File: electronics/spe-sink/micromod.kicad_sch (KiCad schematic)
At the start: 5 parts, among them IC1 AT24C02C-SSHM, X2 MICROMOD_FUNCTION_BOARD_EDGE

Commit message: PD function board schematic progress
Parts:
- C20: footprint CAPC1608* -> Applidyne_Capacitor:CAPC1608X90N
- X2: footprint (none) -> Applidyne_Connector:M.2-MICROMOD-FN-CARD-EDGE
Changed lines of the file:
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@@
       (effects (font (size 1.524 1.524) bold))
     )
-    (property "Footprint" "" (at 156.21 157.48 0)
+    (property "Footprint" "Applidyne_Connector:M.2-MICROMOD-FN-CARD-EDGE" (at 156.21 157.48 0)
       (effects (font (size 0.9906 0.9906)) (justify left bottom) hide)
     )
@@
       (effects (font (size 0.889 0.889)) (justify left))
     )
-    (property "Footprint" "CAPC1608*" (at 61.849 67.31 90)
+    (property "Footprint" "Applidyne_Capacitor:CAPC1608X90N" (at 61.849 67.31 90)
       (effects (font (size 0.508 0.508)) hide)
     )

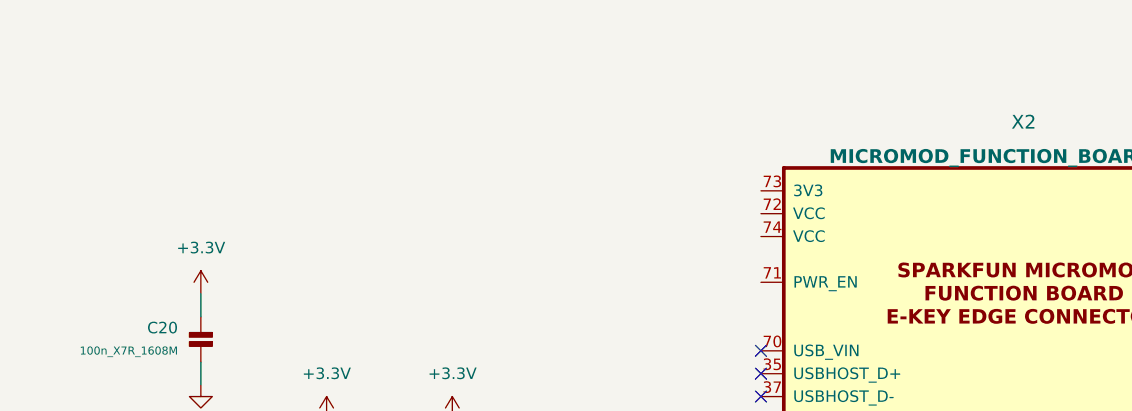
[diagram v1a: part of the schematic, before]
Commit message: PD function board bulk regulator, cleanup, part placement
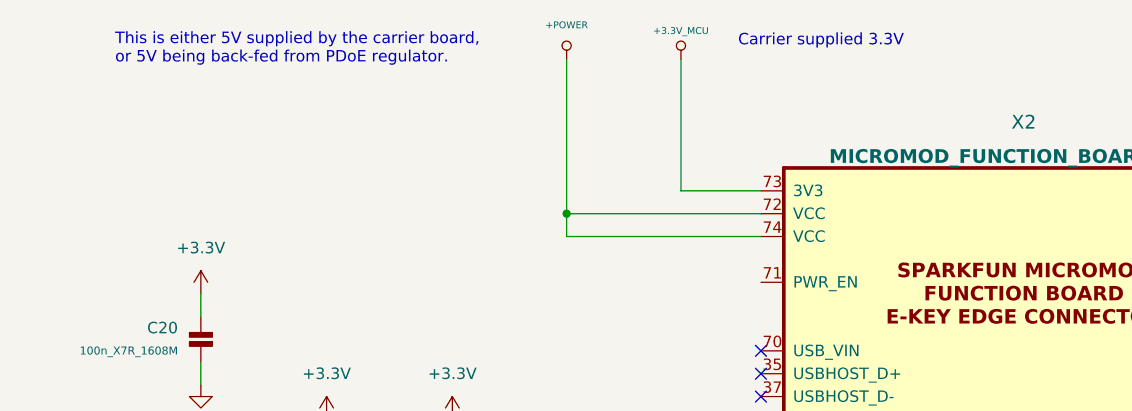
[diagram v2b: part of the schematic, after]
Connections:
- net +POWER: now reaches X2.72 (VCC)
- net +POWER: now also X2.74 (VCC)
- net +3.3V_MCU: now reaches X2.73 (3V3)
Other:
- note added: "Carrier supplied 3.3V"
- note added: "This is either 5V supplied by the carrier board, or 5V being back-fed from PDoE regulator."
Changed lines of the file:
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@@
   (junction (at 123.19 121.92) (diameter 0) (color 0 0 0 0)
+  )
+  (junction (at 105.41 53.34) (diameter 0) (color 0 0 0 0)
   )
   (junction (at 92.71 97.79) (diameter 0) (color 0 0 0 0)
@@
     (stroke (width 0) (type default))
   )
+  (wire (pts (xy 105.41 53.34) (xy 127 53.34))
+    (stroke (width 0) (type default))
+  )
   (wire (pts (xy 185.42 116.84) (xy 215.9 116.84))
     (stroke (width 0) (type default))
@@
     (stroke (width 0) (type default))
   )
+  (wire (pts (xy 127 50.8) (xy 118.11 50.8))
+    (stroke (width 0) (type default))
+  )
   (wire (pts (xy 123.19 129.54) (xy 127 129.54))
     (stroke (width 0) (type default))
@@
     (stroke (width 0) (type default))
   )
+  (wire (pts (xy 118.11 36.195) (xy 118.11 50.8))
+    (stroke (width 0) (type default))
+  )
   (bus (pts (xy 207.01 68.58) (xy 220.98 68.58))
     (stroke (width 0) (type default))
@@
     (stroke (width 0) (type default))
   )
+  (wire (pts (xy 105.41 55.88) (xy 105.41 53.34))
+    (stroke (width 0) (type default))
+  )
+  (wire (pts (xy 105.41 53.34) (xy 105.41 36.195))
+    (stroke (width 0) (type default))
+  )
+  (wire (pts (xy 127 55.88) (xy 105.41 55.88))
+    (stroke (width 0) (type default))
+  )
   (wire (pts (xy 92.71 106.68) (xy 92.71 107.95))
     (stroke (width 0) (type default))
@@
   (bus (pts (xy 207.01 55.88) (xy 207.01 53.34))
     (stroke (width 0) (type default))
+  )
+  (text "Carrier supplied 3.3V" (at 124.46 34.925 0)
+    (effects (font (size 1.27 1.27)) (justify left bottom))
+  )
+  (text "This is either 5V supplied by the carrier board,\nor 5V being back-fed from PDoE regulator."
+    (at 55.245 36.83 0)
+    (effects (font (size 1.27 1.27)) (justify left bottom))
   )
   (text "Write protected when high" (at 119.38 100.33 0)
@@
     )
   )
+  (symbol (lib_id "appli_power:+POWER") (at 105.41 36.195 0) (unit 1)
+    (in_bom yes) (on_board yes) (dnp no) (fields_autoplaced)
+    (property "Reference" "#PWR054" (at 105.41 37.465 0)
+      (effects (font (size 0.508 0.508)) hide)
+    )
+    (property "Value" "+POWER" (at 105.41 32.385 0)
+      (effects (font (size 0.762 0.762)))
+    )
+    (property "Footprint" "" (at 105.41 36.195 0)
+      (effects (font (size 1.524 1.524)))
+    )
+    (property "Datasheet" "" (at 105.41 36.195 0)
+      (effects (font (size 1.524 1.524)))
+    )
+    (pin "1")
+    (instances
+      (project "spe-sink"
+        (path "/f0a501c7-1ad1-4c59-9255-3d6aa4545d8b/d2c298ab-d4a2-4c33-86fb-9b17f2cedd7c"
+          (reference "#PWR054") (unit 1)
+        )
+        (path "/f0a501c7-1ad1-4c59-9255-3d6aa4545d8b/4db035f6-4a09-4a2b-8e2e-a64ccd99d7de"
+          (reference "#PWR024") (unit 1)
+        )
+      )
+    )
+  )
   (symbol (lib_id "appli_power:+3.3V") (at 78.74 76.2 0) (mirror y) (unit 1)
     (in_bom yes) (on_board yes) (dnp no) (fields_autoplaced)
@@
         )
       )
+    )
+  )
+  (symbol (lib_id "appli_power:+3.3V_MCU") (at 118.11 36.195 0) (unit 1)
+    (in_bom yes) (on_board yes) (dnp no) (fields_autoplaced)
+    (property "Reference" "#PWR055" (at 118.11 37.211 0)
+      (effects (font (size 0.762 0.762)) hide)
+    )
+    (property "Value" "+3.3V_MCU" (at 118.11 33.02 0)
+      (effects (font (size 0.762 0.762)))
+    )
+    (property "Footprint" "" (at 118.11 36.195 0)
+      (effects (font (size 1.524 1.524)))
+    )
+    (property "Datasheet" "" (at 118.11 36.195 0)
+      (effects (font (size 1.524 1.524)))
+    )
+    (pin "1")
+    (instances
+      (project "spe-sink"
+        (path "/f0a501c7-1ad1-4c59-9255-3d6aa4545d8b/4db035f6-4a09-4a2b-8e2e-a64ccd99d7de"
+          (reference "#PWR055") (unit 1)
+        )
+      )

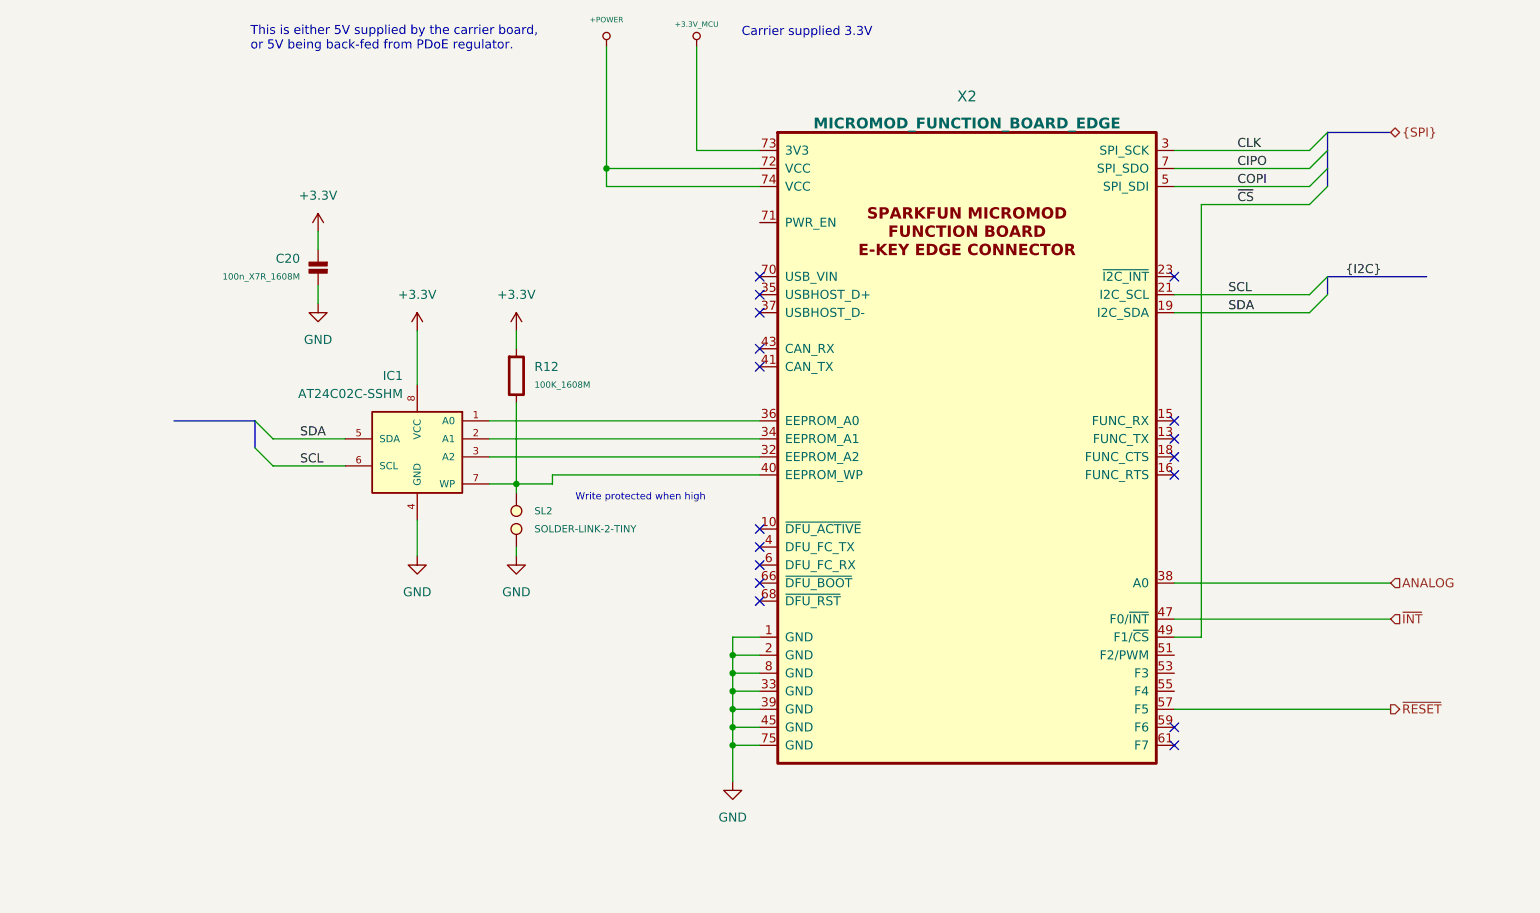
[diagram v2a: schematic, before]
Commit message: PD sink board routing, minor sch changes, etc
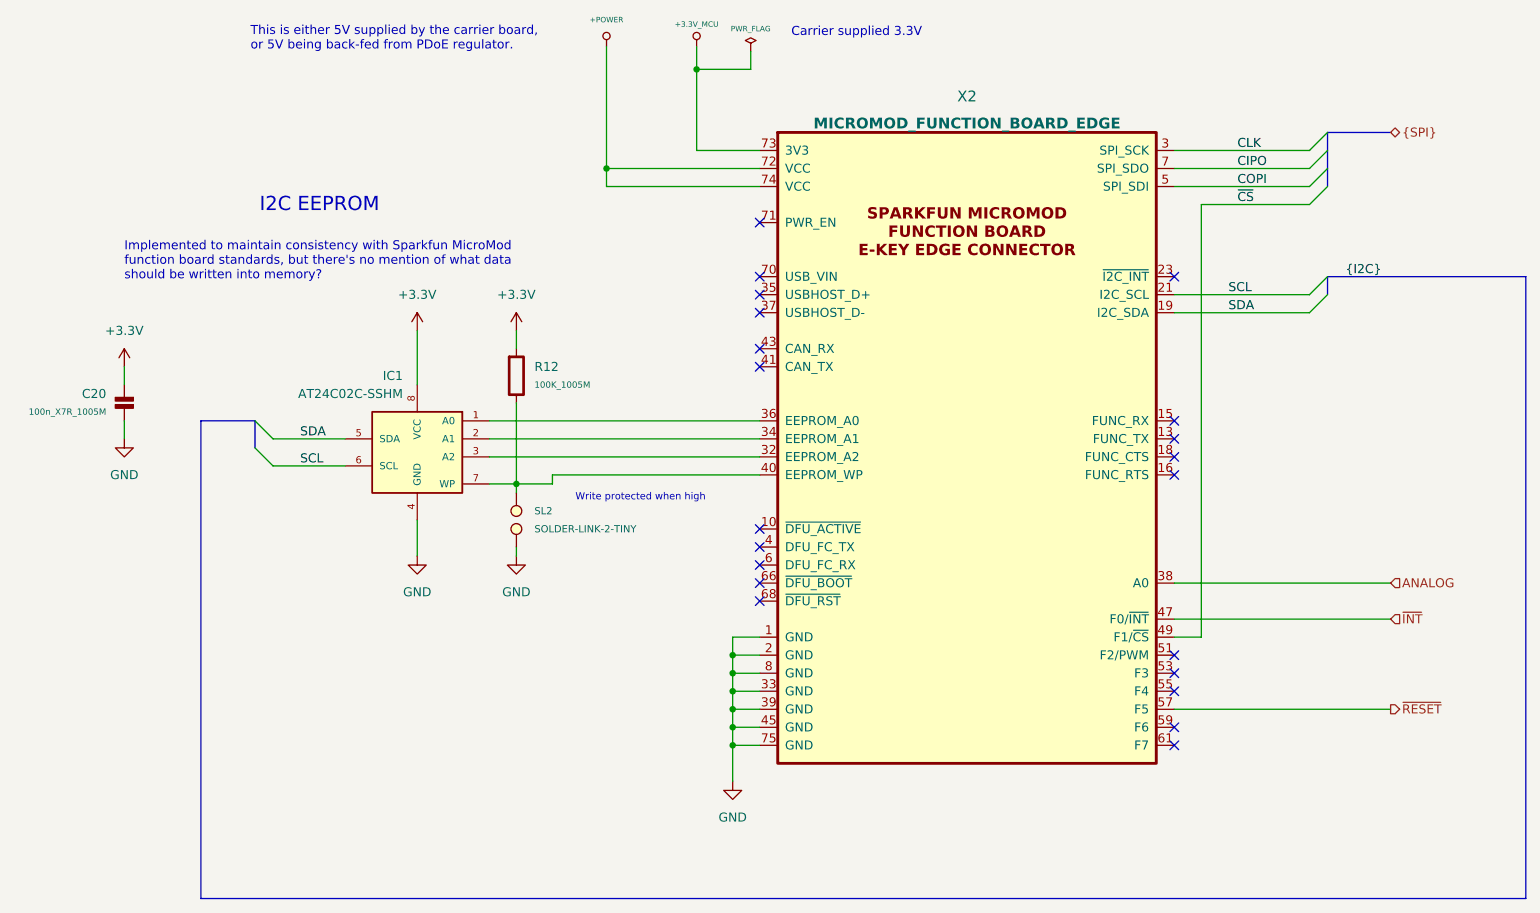
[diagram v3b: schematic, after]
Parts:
- removed C20: 100n_X7R_1608M, Applidyne_Capacitor:CAPC1608X90N, symbol appli_capacitor:100n_X7R_1608M
- removed R12: 100K_1608M, Applidyne_Resistor:RESC1608X50N, symbol appli_resistor:100K_1608M
- added C20: 100n_X7R_1005M, Applidyne_Capacitor:CAPC1005X60N, symbol appli_capacitor:100n_X7R_1005M
- added R12: 100K_1005M, Applidyne_Resistor:RESC1005X40N, symbol appli_resistor:100K_1005M
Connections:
- net +3.3V: now also C20.1, R12.1
- net GND: now also C20.2
- net at IC1.7 (WP), SL2.1, X2.40 (EEPROM_WP): now also R12.2
- no-connect marks 17 -> 21
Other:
- note added: "I2C EEPROM"
- note added: "Implemented to maintain consistency with Sparkfun MicroMod function board standards, but there's no mention of what data should be written into memory?"

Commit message: PD sink PCB design 'finished', page cleanup, etc
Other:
- title: (none) -> MicroMod Function Board
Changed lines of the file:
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@@
 (kicad_sch (version 20230121) (generator eeschema)
   (paper "A4")
+  (title_block
+    (title "MicroMod Function Board")
+    (date "2023-08-16")
+    (rev "V1.0")
+    (comment 2 "Aims to maintain drop-in compatibility with Sparkfun ADIN1110 board")
+    (comment 3 "Edge connector part, build using a 0.8mm PCB")
+  )
   (junction (at 123.19 124.46) (diameter 0) (color 0 0 0 0)
   )
